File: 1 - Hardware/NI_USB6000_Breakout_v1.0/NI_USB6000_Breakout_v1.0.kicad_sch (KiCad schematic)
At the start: 12 parts, among them J1 NI_6000_CONN, J2 2601-1108, J3 2601-1108, J4 2601-1108

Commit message: Mep
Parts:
- added D1: D_Zener, symbol Device:D_Zener
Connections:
- net AIN_0: now also D1.1 (K)
- net GND: now also D1.2 (A)
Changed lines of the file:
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@@
 	)
 	(junction
+		(at 32.385 90.17)
+		(diameter 0)
+		(color 0 0 0 0)
+	)
+	(junction
 		(at 154.94 127.635)
 		(diameter 0)
@@
 		(color 0 0 0 0)
 	)
+	(junction
+		(at 35.56 101.6)
+		(diameter 0)
+		(color 0 0 0 0)
+	)
 	(wire
 		(pts
@@
 	(wire
 		(pts
-			(xy 35.56 90.17) (xy 33.655 90.17)
+			(xy 35.56 90.17) (xy 32.385 90.17)
 		)
 		(stroke
@@
 	(wire
 		(pts
+			(xy 32.385 99.695) (xy 32.385 101.6)
+		)
+		(stroke
+			(width 0)
+			(type default)
+		)
+	)
+	(wire
+		(pts
 			(xy 118.745 125.095) (xy 116.84 125.095)
 		)
@@
 	(wire
 		(pts
+			(xy 32.385 90.17) (xy 32.385 92.075)
+		)
+		(stroke
+			(width 0)
+			(type default)
+		)
+	)
+	(wire
+		(pts
 			(xy 51.435 107.95) (xy 49.53 107.95)
 		)
@@
 	(wire
 		(pts
+			(xy 35.56 103.505) (xy 35.56 101.6)
+		)
+		(stroke
+			(width 0)
+			(type default)
+		)
+	)
+	(wire
+		(pts
 			(xy 83.185 120.65) (xy 85.09 120.65)
 		)
@@
 	(wire
 		(pts
+			(xy 32.385 101.6) (xy 35.56 101.6)
+		)
+		(stroke
+			(width 0)
+			(type default)
+		)
+	)
+	(wire
+		(pts
 			(xy 116.84 97.155) (xy 116.84 99.695)
 		)
@@
 	(wire
 		(pts
+			(xy 32.385 90.17) (xy 30.48 90.17)
+		)
+		(stroke
+			(width 0)
+			(type default)
+		)
+	)
+	(wire
+		(pts
 			(xy 118.745 107.315) (xy 116.84 107.315)
 		)
@@
 	(global_label "AIN_0"
 		(shape input)
-		(at 33.655 90.17 180)
+		(at 30.48 90.17 180)
 		(fields_autoplaced yes)
 		(effects
@@
 		)
 		(property "Intersheetrefs" "${INTERSHEET_REFS}"
-			(at 25.4688 90.17 0)
+			(at 22.2938 90.17 0)
 			(effects
 				(font
@@
 	(symbol
 		(lib_id "power:GND")
-		(at 35.56 101.6 0)
+		(at 35.56 103.505 0)
 		(unit 1)
 		(exclude_from_sim no)
@@
 		(fields_autoplaced yes)
 		(property "Reference" "#PWR03"
-			(at 35.56 107.95 0)
+			(at 35.56 109.855 0)
 			(effects
 				(font
@@
 		)
 		(property "Value" "GND"
-			(at 35.56 106.045 0)
+			(at 35.56 107.95 0)
 			(effects
 				(font
@@
 		)
 		(property "Footprint" ""
-			(at 35.56 101.6 0)
+			(at 35.56 103.505 0)
 			(effects
 				(font
@@
 		)
 		(property "Datasheet" ""
-			(at 35.56 101.6 0)
+			(at 35.56 103.505 0)
 			(effects
 				(font
@@
 		)
 		(property "Description" "Power symbol creates a global label with name \"GND\" , ground"
-			(at 35.56 101.6 0)
+			(at 35.56 103.505 0)
 			(effects
 				(font
@@
 					(unit 1)
 				)
+			)
+		)
+	)
+	(symbol
+		(lib_id "Device:D_Zener")
+		(at 32.385 95.885 90)
+		(mirror x)
+		(unit 1)
+		(exclude_from_sim no)
+		(in_bom yes)
+		(on_board yes)
+		(dnp no)
+		(property "Reference" "D1"
+			(at 29.21 94.6149 90)
+			(effects
+				(font
+					(size 1.27 1.27)
+				)
+				(justify left)
+			)
+		)
+		(property "Value" "D_Zener"
+			(at 29.21 97.1549 90)
+			(effects
+				(font
+					(size 1.27 1.27)
+				)
+				(justify left)
+			)
+		)
+		(property "Footprint" ""
+			(at 32.385 95.885 0)
+			(effects
+				(font
+					(size 1.27 1.27)
+				)
+				(hide yes)
+			)
+		)
+		(property "Datasheet" "~"
+			(at 32.385 95.885 0)
+			(effects
+				(font
+					(size 1.27 1.27)
+				)
+				(hide yes)
+			)
+		)
+		(property "Description" "Zener diode"
+			(at 32.385 95.885 0)
+			(effects
+				(font
+					(size 1.27 1.27)
+				)
+				(hide yes)
+			)
+		)
+		(pin "1"
+		)
+		(pin "2"
+		)
+		(instances
+			(project ""
+				(path "/40e6b734-6f82-4eb0-ba0b-f1bb8be34735"
+					(reference "D1")
+					(unit 1)
+				)

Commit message: Work
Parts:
- removed D1: D_Zener, symbol Device:D_Zener
- added D1, D2, D3, D4: SZMMBZ12VALT1G, Package_TO_SOT_SMD:SOT-23-3, symbol Device:D_Zener_Dual_CommonAnode_KKA
- added J5: AIN_PWR_IN, 2602_1102:CONN2_2601-1102_WAG, symbol 2602_1102:2601-1102
- added Q1: Q_NMOS_Depletion_DGS, symbol Transistor_FET_Other:Q_NMOS_Depletion_DGS
- added R9: R, symbol Device:R
- J2: value 2601-1108 -> AIN_CONN
- J3: value 2601-1108 -> PWR_CONN
- J4: value 2601-1108 -> GND_CONN
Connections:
- net AIN_0: now also D1.1 (K)
- net AIN_1: now also D1.2 (K)
- net AIN_2: now also D2.1 (K)
- net AIN_3: now also D2.2 (K)
- net AIN_4: now also D3.1 (K)
- net AIN_5: now also D3.2 (K)
- net AIN_6: now also D4.1 (K)
- net AIN_7: now also D4.2 (K)
- net GND: now also D1.3 (A), D2.3 (A), D3.3 (A), D4.3 (A), J5.1 (1_1), J5.2 (1_2)
- net PFIO_0: now also R9.1
- net SENSOR_PWR: now also J5.3 (2_1), J5.4 (2_2)
- new net: Q1.2 (G), R9.2
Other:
- moved on the sheet: J2, J3, J4, R1, R2

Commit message: USB 6000 Breakout work
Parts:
- removed Q1: Q_NMOS_Depletion_DGS, symbol Transistor_FET_Other:Q_NMOS_Depletion_DGS
- removed R9: R, symbol Device:R
- added D5: LED, symbol Device:LED
- added J6: CONTROL_PWR_IN, WAGO_2601_1104:CONN4_2601-1104_WAG, symbol WAGO_2601_1104:2601-1104
- added J7, J8: CONTROL PWR, CONN4_2601-3104_WAG, symbol 2601_3104:2601-3104
- added Q1, Q2, Q3, Q4: GSFD6016, Package_TO_SOT_SMD:TO-252-2, symbol Transistor_FET:Q_NMOS_GDS
- added R10, R12, R14, R16: 10k, symbol Device:R
- added R17: R, symbol Device:R
- added R9: YC164-FR-0710RL, YC164_FR_0710RZ:RESCAXE80P320X160X70-8N, symbol YC164_FR_0710RZ:YC164-FR-0710RL
- added U1: MIC4469YN, MIC4469YN:PDIP-14_MCL, symbol MIC4469YN:MIC4469YN
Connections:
- net GND: now also D5.1 (K), J6.1 (1_1), J6.2 (1_2), Q1.3 (S), Q2.3 (S), Q3.3 (S), Q4.3 (S), R10.1, R12.1, R14.1, R16.1, U1.2 (1B), U1.4 (2B), U1.6 (3B), U1.7 (GND), U1.9 (4B)
- net PFIO_0: now also U1.1 (1A)
- net PFIO_1: now also U1.3 (2A)
- net PFIO_2: now also U1.5 (3A)
- net PFIO_3: now also U1.8 (4A)
- net SENSOR_PWR: now also R17.1
- new net: Q4.1 (G), R16.2, R9.5
- new net: Q3.1 (G), R14.2, R9.6
- new net: Q2.1 (G), R12.2, R9.7
- new net: Q1.1 (G), R10.2, R9.8
- new net: D5.2 (A), R17.2
- new net: J6.3 (2_1), J6.4 (2_2), J6.5 (3_1), J6.6 (3_2)
- new net +12V: U1.14 (VS)
- new net CONTROL_PWR: J6.7 (4_1), J6.8 (4_2), J7.1 (1_1), J7.2 (1_2), J7.3 (2_1), J7.4 (2_2), J7.5 (3_1), J7.6 (3_2), J7.7 (4_1), J7.8 (4_2)
- new net DRAIN_1: J8.1 (1_1), J8.2 (1_2), Q1.2 (D)
- new net DRAIN_2: J8.3 (2_1), J8.4 (2_2), Q2.2 (D)
- new net DRAIN_3: J8.5 (3_1), J8.6 (3_2), Q3.2 (D)
- new net DRAIN_4: J8.7 (4_1), J8.8 (4_2), Q4.2 (D)
- new net GATE_1: R9.1, U1.13 (1Y)
- new net GATE_2: R9.2, U1.12 (2Y)
- new net GATE_3: R9.3, U1.11 (3Y)
- new net GATE_4: R9.4, U1.10 (4Y)
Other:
- note added: "10 OHM"
- note added: "SWITCH REQUIRED"
- moved on the sheet: D1, D2, D3, D4, J1, J2, J3, J4, J5, R1, R2, R3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

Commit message: USB 6000 KiCAD Work
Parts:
- removed D5: LED, symbol Device:LED
- added D10, D6, D7, D9: D, symbol Device:D
- added D11, D12, D5, D8: D_Zener, symbol Device:D_Zener
- added D13, D14: LED, symbol Device:LED
- added R15: R, symbol Device:R
- added TP1, TP10, TP11, TP12, TP13, TP14, TP15, TP16, TP17, TP18, TP19, TP2, TP20, TP21, TP22, TP23, TP3, TP4, TP5, TP6, TP7, TP8, TP9: TestPoint, symbol Connector:TestPoint
- renumbered R12 to R11, R14 to R12, R16 to R13, R17 to R14
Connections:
- net AIN_0: now also TP4.1
- net AIN_1: now also TP5.1
- net AIN_2: now also TP6.1
- net AIN_3: now also TP7.1
- net AIN_4: now also TP8.1
- net AIN_5: now also TP9.1
- net AIN_6: now also TP10.1
- net AIN_7: now also TP11.1
- net CONTROL_PWR: now also D11.2 (A), D12.2 (A), D5.2 (A), D8.2 (A), R15.1, TP3.1
- net DRAIN_1: now also D6.2 (A), TP20.1
- net DRAIN_2: now also D7.2 (A), TP21.1
- net DRAIN_3: now also D9.2 (A), TP22.1
- net DRAIN_4: now also D10.2 (A), TP23.1
- net GATE_1: now also TP16.1
- net GATE_2: now also TP17.1
- net GATE_3: now also TP18.1
- net GATE_4: now also TP19.1
- net GND: now also D13.1 (K), D14.1 (K), TP1.1
- net PFIO_0: now also TP12.1
- net PFIO_1: now also TP13.1
- net PFIO_2: now also TP14.1
- net PFIO_3: now also TP15.1
- net SENSOR_PWR: now also TP2.1
- net at R14.2: now also D13.2 (A)
- new net: D10.1 (K), D12.1 (K)
- new net: D11.1 (K), D9.1 (K)
- new net: D14.2 (A), R15.2
- new net: D7.1 (K), D8.1 (K)
- new net: D5.1 (K), D6.1 (K)
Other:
- note added: "AIN CONNS"
- note added: "CLAMPING DIODE CIRCUITRY"
- note added: "CONTROL CONNS"
- note added: "CURRENT IN CIRCUITRY"
- note added: "Horz."
- note added: "INDICATION LEDS"
- note added: "MOSFET DRIVER"
- note added: "TEST POINTS"
- note added: "USB 6000 CONN"
- note added: "Vert."
- moved on the sheet: D1, D2, D3, D4, J1, J2, J3, J4, J5, J6, J7, J8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

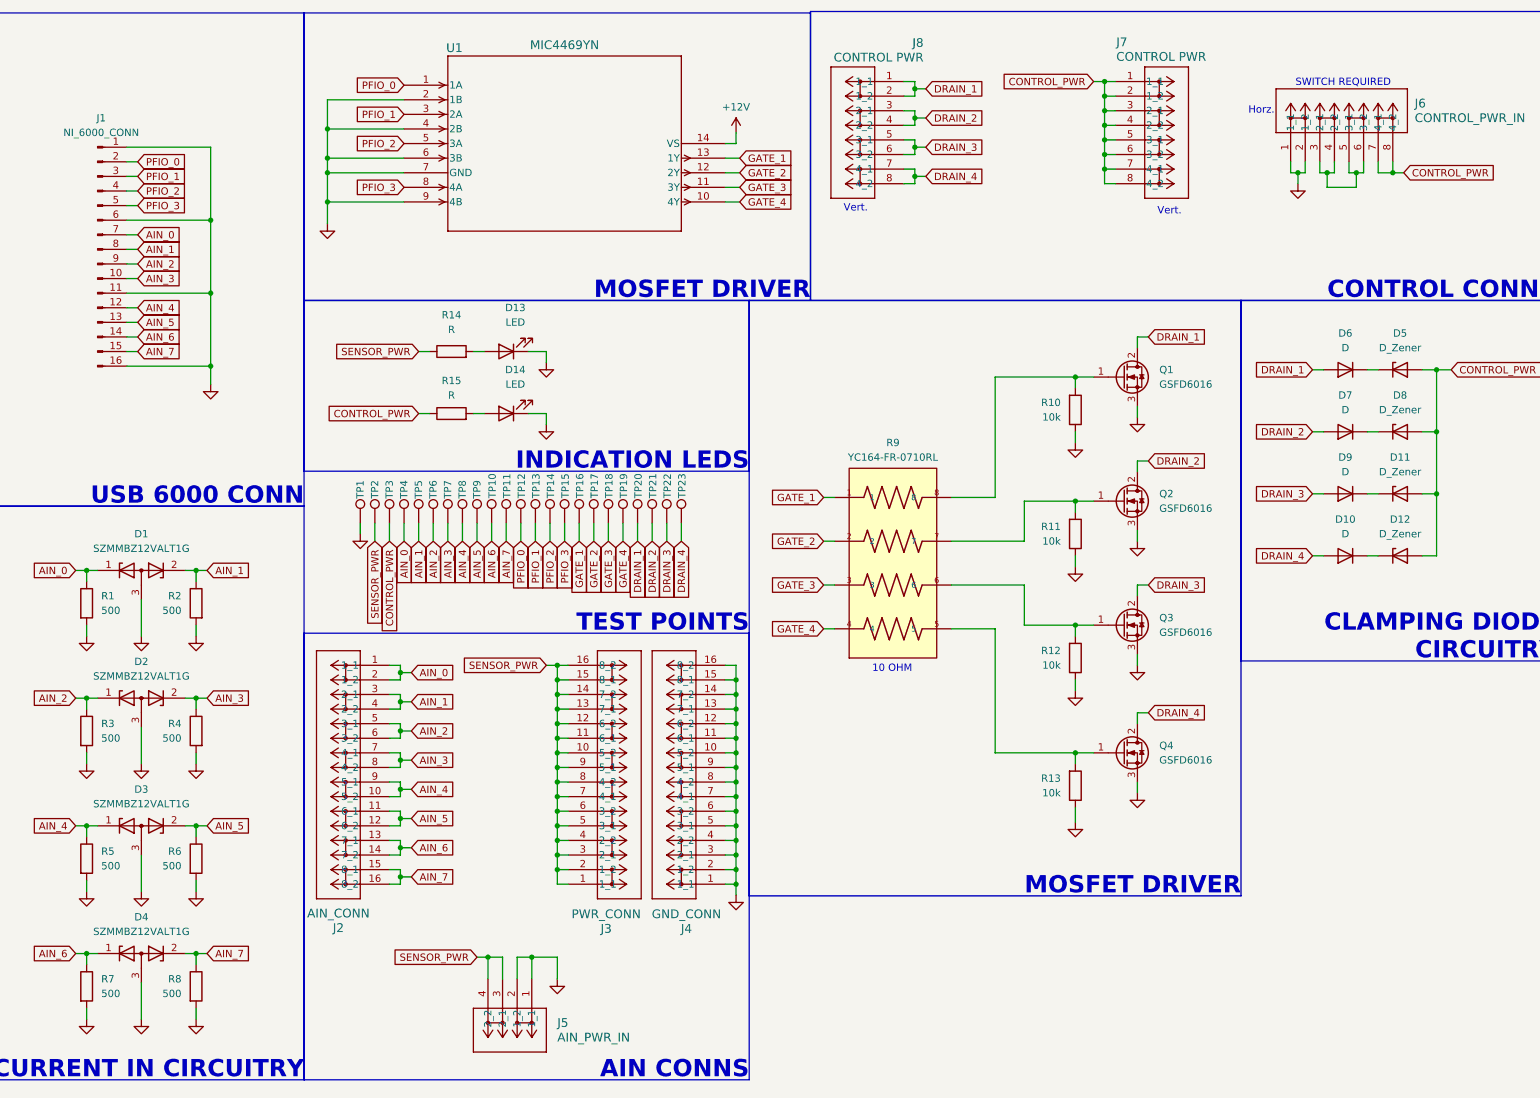
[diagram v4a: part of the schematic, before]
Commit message: USB 6000 Breakout Board and code shuffling
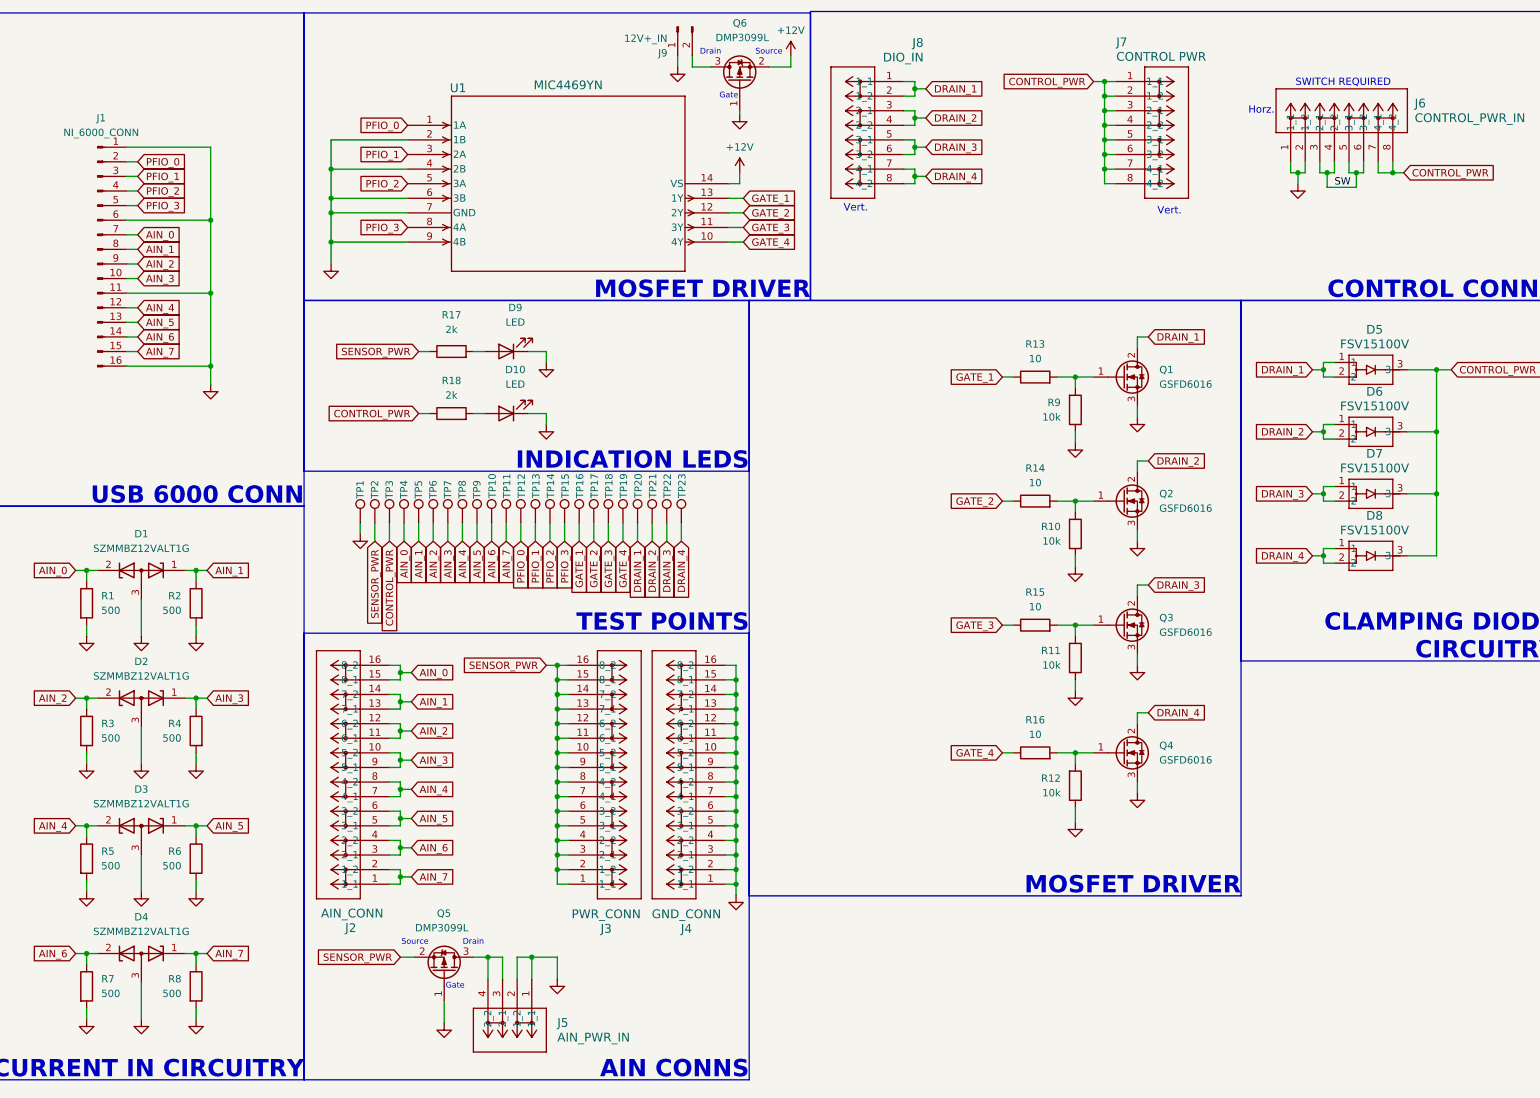
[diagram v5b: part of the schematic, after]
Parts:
- removed D10, D6, D7, D9: D, symbol Device:D
- removed D11, D12, D5, D8: D_Zener, symbol Device:D_Zener
- removed R9: YC164-FR-0710RL, YC164_FR_0710RZ:RESCAXE80P320X160X70-8N, symbol YC164_FR_0710RZ:YC164-FR-0710RL
- added D5, D6, D7, D8: FSV15100V, FSV15100V:TO-277-3LD_ONS, symbol FSV15100V:FSV15100V
- added J9: 12V+_IN, Connector_PinHeader_2.54mm:PinHeader_1x02_P2.54mm_Vertical, symbol Connector:Conn_01x02_Pin
- added Q5, Q6: DMP3099L, Package_TO_SOT_SMD:SOT-23-3, symbol Device:Q_PMOS_GSD
- added R13, R14, R15, R16: 10, Resistor_SMD:R_1206_3216Metric, symbol Device:R
- D10: renamed from D14; footprint (none) -> LED_SMD:LED_1206_3216Metric
- D9: renamed from D13; footprint (none) -> LED_SMD:LED_1206_3216Metric
- J1: footprint Connector_PinHeader_2.54mm:PinHeader_1x16_P2.54mm_Horizontal -> 759000421:3.5mmPitch01x16
- J2, J3, J4: footprint CONN8_2601-1108_WAG -> WAGO_2601_3108:CONN8_2601-3108_WAG; symbol 2601-3108:2601-1108 -> WAGO_2601_3108:2601-3108
- J5: footprint 2602_1102:CONN2_2601-1102_WAG -> WAGO_2601_1102:CONN2_2601-1102_WAG
- J7: footprint CONN4_2601-3104_WAG -> 2601_3104:CONN4_2601-3104_WAG
- J8: value CONTROL PWR -> DIO_IN; footprint CONN4_2601-3104_WAG -> 2601_3104:CONN4_2601-3104_WAG
- R1, R2, R3, R4, R5, R6, R7, R8: footprint (none) -> Resistor_SMD:R_0603_1608Metric
- R10: renamed from R11; footprint (none) -> Resistor_SMD:R_1206_3216Metric
- R11: renamed from R12; footprint (none) -> Resistor_SMD:R_1206_3216Metric
- R12: renamed from R13; footprint (none) -> Resistor_SMD:R_1206_3216Metric
- R17: renamed from R14; value R -> 2k; footprint (none) -> Resistor_SMD:R_1206_3216Metric
- R18: renamed from R15; value R -> 2k; footprint (none) -> Resistor_SMD:R_1206_3216Metric
- R9: renamed from R10; footprint (none) -> Resistor_SMD:R_1206_3216Metric
- TP1, TP10, TP11, TP12, TP13, TP14, TP15, TP16, TP17, TP18, TP19, TP2, TP20, TP21, TP22, TP23, TP3, TP4, TP5, TP6, TP7, TP8, TP9: footprint (none) -> TestPoint:TestPoint_THTPad_D2.0mm_Drill1.0mm
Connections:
- net +12V: now also Q6.2 (S)
- net AIN_0: now also D1.2 (K), J2.15 (8_1), J2.16 (8_2); no longer D1.1 (K), J2.1 (1_1), J2.2 (1_2)
- net AIN_1: now also D1.1 (K), J2.13 (7_1), J2.14 (7_2); no longer D1.2 (K), J2.3 (2_1), J2.4 (2_2)
- net AIN_2: now also D2.2 (K), J2.11 (6_1), J2.12 (6_2); no longer D2.1 (K), J2.5 (3_1), J2.6 (3_2)
- net AIN_3: now also D2.1 (K), J2.10 (5_2), J2.9 (5_1); no longer D2.2 (K), J2.7 (4_1), J2.8 (4_2)
- net AIN_4: now also D3.2 (K), J2.7 (4_1), J2.8 (4_2); no longer D3.1 (K), J2.10 (5_2), J2.9 (5_1)
- net AIN_5: now also D3.1 (K), J2.5 (3_1), J2.6 (3_2); no longer D3.2 (K), J2.11 (6_1), J2.12 (6_2)
- net AIN_6: now also D4.2 (K), J2.3 (2_1), J2.4 (2_2); no longer D4.1 (K), J2.13 (7_1), J2.14 (7_2)
- net AIN_7: now also D4.1 (K), J2.1 (1_1), J2.2 (1_2); no longer D4.2 (K), J2.15 (8_1), J2.16 (8_2)
- net CONTROL_PWR: now also D5.3, D6.3, D7.3, D8.3
- net DRAIN_1: now also D5.1, D5.2
- net DRAIN_2: now also D6.1, D6.2
- net DRAIN_3: now also D7.1, D7.2
- net DRAIN_4: now also D8.1, D8.2
- net GATE_1: now also R13.1
- net GATE_2: now also R14.1
- net GATE_3: now also R15.1
- net GATE_4: now also R16.1
- net GND: now also J9.1 (Pin_1), Q5.1 (G), Q6.1 (G)
- net SENSOR_PWR: now also Q5.2 (S); no longer J5.3 (2_1), J5.4 (2_2)
- net at Q4.1 (G), R12.2: now also R16.2
- net at Q3.1 (G), R11.2: now also R15.2
- net at Q2.1 (G), R10.2: now also R14.2
- net at Q1.1 (G), R9.2: now also R13.2
- net SW: now reaches J6.3 (2_1), J6.4 (2_2), J6.5 (3_1), J6.6 (3_2)
- new net: J5.3 (2_1), J5.4 (2_2), Q5.3 (D)
- new net: J9.2 (Pin_2), Q6.3 (D)
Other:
- note added: "Drain"
- note added: "Gate"
- note added: "Source"
- note removed: "10 OHM"
- moved on the sheet: J2, U1
